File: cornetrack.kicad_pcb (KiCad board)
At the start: 2 copper layers, 275.5 x 114.5 mm, 186 parts, among them J1 MJ-4PP-9, J2 OLED, J3 MJ-4PP-9, J4 OLED, SW1 SW_PUSH, SW10 SW_PUSH, SW11 SW_PUSH, SW12 SW_PUSH, SW13 SW_PUSH, SW14 SW_PUSH, SW15 SW_PUSH, SW16 SW_PUSH, SW17 SW_PUSH, SW18 SW_PUSH, SW19 SW_PUSH, SW2 SW_PUSH, SW20 SW_PUSH, SW21 SW_PUSH, SW22 SW_PUSH, SW23 SW_PUSH, SW24 SW_PUSH, SW25 SW_PUSH, SW26 SW_PUSH, SW27 SW_PUSH, SW28 SW_PUSH, SW29 SW_PUSH, SW3 SW_PUSH, SW30 SW_PUSH, SW31 SW_PUSH, SW32 SW_PUSH, SW33 SW_PUSH, SW34 SW_PUSH, SW35 SW_PUSH, SW36 SW_PUSH, SW37 SW_PUSH, SW38 SW_PUSH, SW39 SW_PUSH, SW4 SW_PUSH, SW40 SW_PUSH, SW41 SW_PUSH, SW42 SW_PUSH, SW43 SW_PUSH, SW44 SW_PUSH, SW45 SW_PUSH, SW46 SW_PUSH, SW47 SW_PUSH, SW48 SW_PUSH, SW5 SW_PUSH, SW6 SW_PUSH, SW7 SW_PUSH, SW8 SW_PUSH, SW9 SW_PUSH, U1 ProMicro, U2 ProMicro

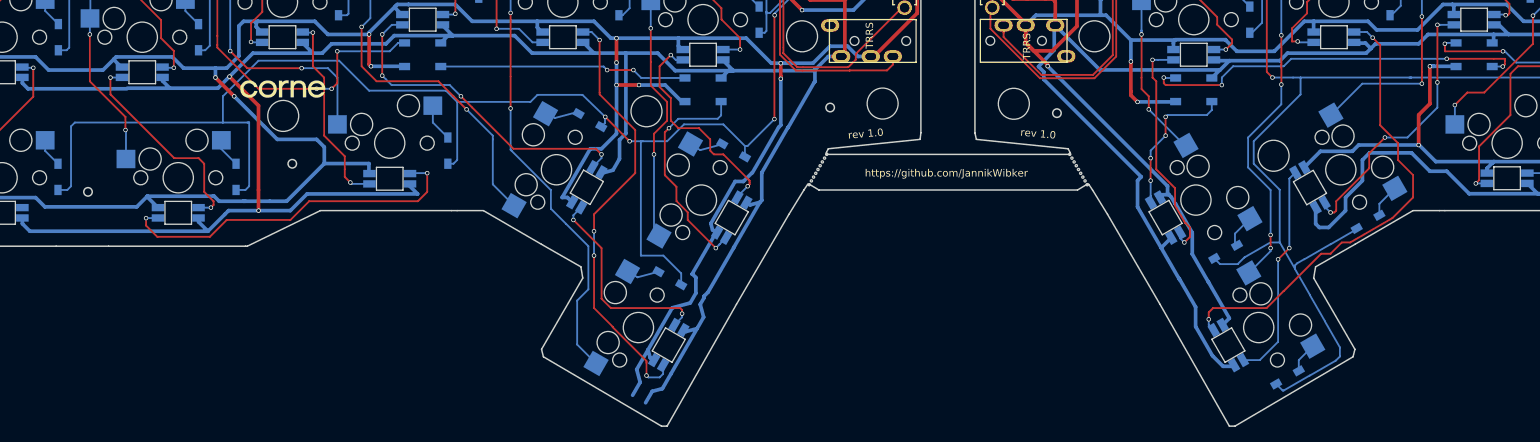
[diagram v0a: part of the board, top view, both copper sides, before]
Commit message: renamed project, diode rotation, assembly - renamed project from corne-cherry to cornetrack - tried to have all diodes rotated the same way - did numerous assembly related shenanigans; this is all in an attempt to get jlcpcb to properly detect component orientation
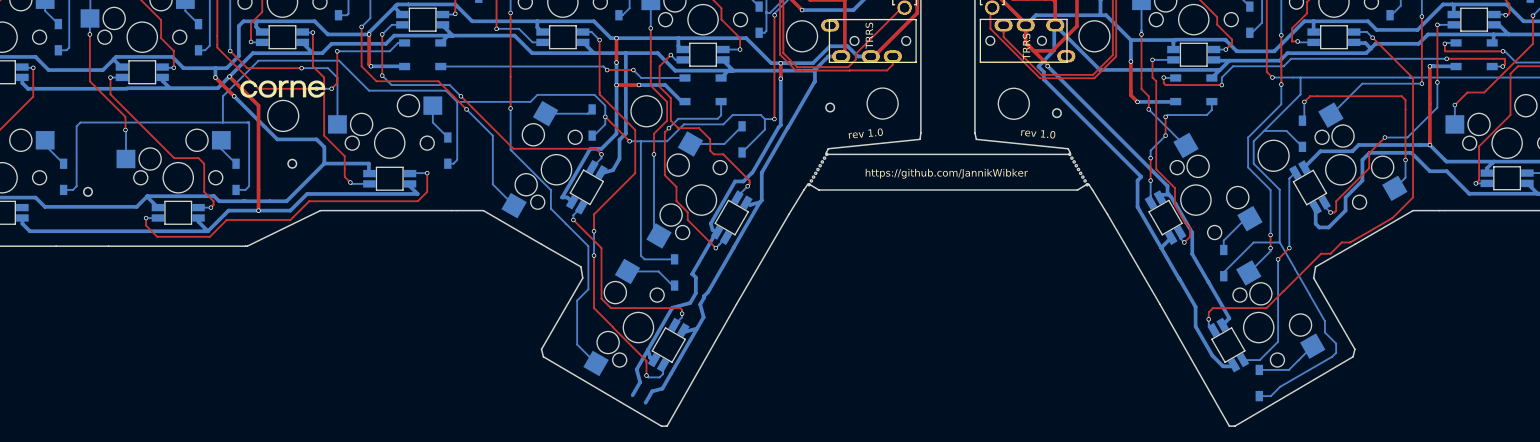
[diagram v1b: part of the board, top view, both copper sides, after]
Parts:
- moved D40 14.9 mm to (196.3, 86.9), turned to 90 degrees
- moved D41 3.89 mm to (190.5, 120.7), turned to 90 degrees
- moved D21 1.87 mm to (120.4, 87.6), turned to 90 degrees
- moved D42 1.55 mm to (185.7, 104.4), turned to 90 degrees
- moved D20 1.01 mm to (111.3, 105.7), turned to 270 degrees
- moved D43 0.76 mm to (28.4, 92.7)
- moved D19 0.44 mm to (100.1, 85.3), turned to 90 degrees
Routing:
- net Net-(D40-Pad2): track 4.52 -> 29.5 mm, vias 0 -> 2
- net Net-(D41-Pad2): track 4.13 -> 8.57 mm
- net Net-(D21-Pad2): track 4.62 -> 7.99 mm
- net row3_r: track 241.1 -> 238.3 mm
- net Net-(D20-Pad2): track 4.51 -> 7.17 mm
- net Net-(D19-Pad2): track 4.80 -> 6.55 mm
- net Net-(D42-Pad2): track 4.56 -> 6.06 mm
- net row3: track 212.5 -> 213.8 mm
- net GNDA: track 726.5 -> 725.9 mm

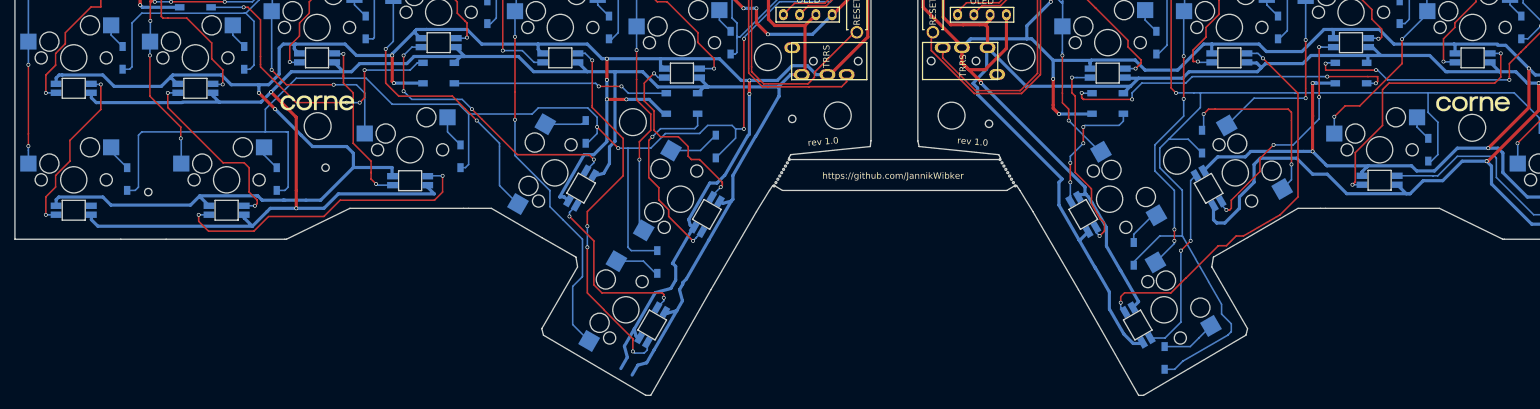
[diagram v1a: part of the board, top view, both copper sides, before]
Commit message: added bottom-plate as subproject (has no real schematic; only pcb)
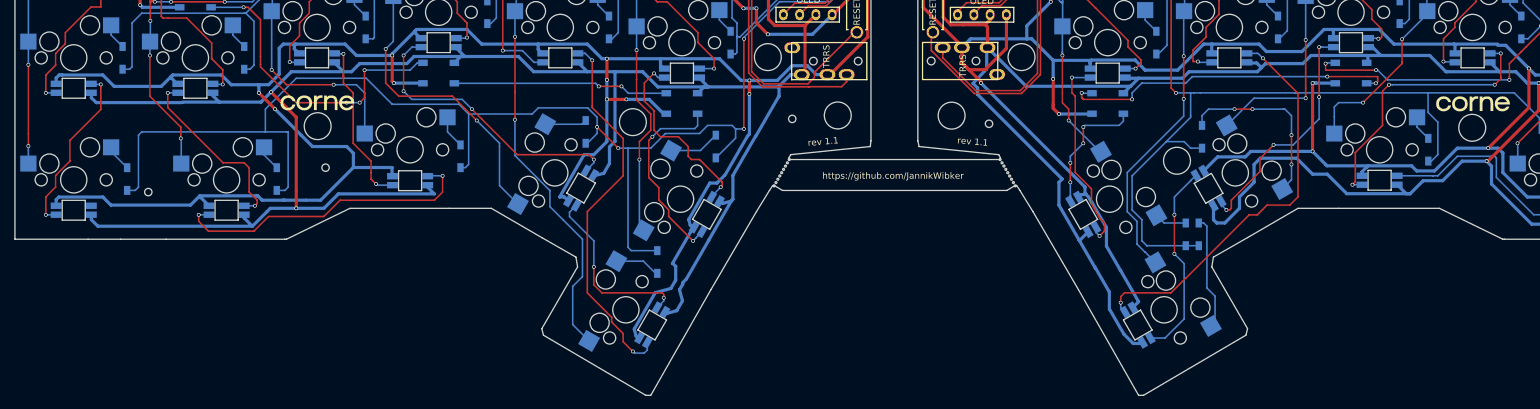
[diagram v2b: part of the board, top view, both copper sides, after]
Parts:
- added ?: , , F.Cu at (142.7, 185.2)
- moved D41 20.0 mm to (195.8, 101.3)
- moved D42 8.68 mm to (193.8, 101.3)
- moved D40 0.76 mm to (196.3, 86.1)
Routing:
- net row3_r: track 238.3 -> 209.4 mm
- net VCC: track 610.7 -> 598.1 mm
- net Net-(D41-Pad2): track 8.57 -> 17.8 mm
- net GND: track 725.7 -> 718.8 mm
- net Net-(LED52-Pad4): track 29.7 -> 31.0 mm
- net col4_r: track 130.4 -> 131.5 mm, vias 8 -> 6
- net Net-(D40-Pad2): track 29.5 -> 28.4 mm, vias 2 -> 4
- net Net-(D42-Pad2): track 6.06 -> 5.07 mm
- net col2_r: track 159.1 -> 160.0 mm
- net Net-(LED48-Pad2): vias 2 -> 4
- net Net-(LED23-Pad2): vias 4 -> 2
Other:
- outline, holes or cut-outs redrawn
- board text added: "rev 1.1"
- board text removed: "rev 1.0"

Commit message: regenerated gerber files
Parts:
- moved D21 19.5 mm to (105.4, 100.1)
- moved D20 9.66 mm to (103.4, 100.1), turned to 90 degrees
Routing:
- net row3: track 213.8 -> 204.5 mm, vias 4 -> 6
- net Net-(D21-Pad2): track 7.99 -> 16.9 mm
- net Net-(D20-Pad2): track 7.17 -> 10.2 mm
- net Net-(LED24-Pad4): track 30.3 -> 27.9 mm
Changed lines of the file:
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@@
-(kicad_pcb (version 20171130) (host pcbnew "(5.1.6-0-10_14)")
+(kicad_pcb (version 20171130) (host pcbnew "(5.1.5-rc2)")
   (general
     (thickness 1.6)
     (drawings 351)
-    (tracks 3212)
+    (tracks 3214)
     (zones 0)
     (modules 187)
@@
       (drillshape 0)
       (scaleselection 1)
-      (outputdirectory "assembly/"))
+      (outputdirectory "./"))
   )
   (net 0 "")
@@
   (module "" (layer F.Cu)
     (at 142.748 185.166)
+    (attr smd)
     (fp_text reference "" (at 145.288 185.42) (layer F.SilkS)
       (effects (font (size 1.27 1.27) (thickness 0.15)))
@@
   )
   (module kbd:D3_SMD_v2 (layer B.Cu)
-    (at 111.252 105.664 270)
+    (at 103.378 100.076 90)
     (descr "Resitance 3 pas")
     (tags R)
@@
     (fp_line (start 2.7 0.75) (end -2.7 0.75) (layer B.SilkS) (width 0.15))
     (fp_line (start -2.7 -0.75) (end 2.7 -0.75) (layer B.SilkS) (width 0.15))
-    (pad 2 smd rect (at 1.775 0 270) (size 1.4 1) (layers B.Cu B.Paste B.Mask)
+    (pad 2 smd rect (at 1.775 0 90) (size 1.4 1) (layers B.Cu B.Paste B.Mask)
       (net 24 "Net-(D20-Pad2)"))
-    (pad 1 smd rect (at -1.775 0 270) (size 1.4 1) (layers B.Cu B.Paste B.Mask)
+    (pad 1 smd rect (at -1.775 0 90) (size 1.4 1) (layers B.Cu B.Paste B.Mask)
       (net 7 row3))
     (model ${KIGITHUB3D}/Diode_SMD.3dshapes/D_SOD-123.step
@@
   )
   (module kbd:D3_SMD_v2 (layer B.Cu)
-    (at 120.396 87.63 90)
+    (at 105.41 100.076 90)
     (descr "Resitance 3 pas")
     (tags R)
@@
   (segment (start 100.333 87.119) (end 101.854 85.598) (width 0.25) (layer B.Cu) (net 7))
   (segment (start 100.076 87.119) (end 100.333 87.119) (width 0.25) (layer B.Cu) (net 7))
-  (segment (start 123.487999 84.879999) (end 124.782499 84.879999) (width 0.25) (layer B.Cu) (net 7))
-  (segment (start 119.126 84.328) (end 122.936 84.328) (width 0.25) (layer B.Cu) (net 7))
+  (segment (start 106.68 87.884) (end 106.68 93.541) (width 0.25) (layer B.Cu) (net 7))
+  (segment (start 124.064498 85.598) (end 124.782499 84.879999) (width 0.25) (layer B.Cu) (net 7))
+  (segment (start 112.522 85.598) (end 124.064498 85.598) (width 0.25) (layer B.Cu) (net 7))
   (segment (start 110.236 87.884) (end 112.522 85.598) (width 0.25) (layer B.Cu) (net 7))
-  (segment (start 117.856 85.598) (end 119.126 84.328) (width 0.25) (layer B.Cu) (net 7))
-  (segment (start 122.936 84.328) (end 123.487999 84.879999) (width 0.25) (layer B.Cu) (net 7))
-  (segment (start 112.522 85.598) (end 117.856 85.598) (width 0.25) (layer B.Cu) (net 7))
   (segment (start 105.156 87.884) (end 110.236 87.884) (width 0.25) (layer B.Cu) (net 7))
-  (segment (start 123.487999 86.313001) (end 120.396 89.405) (width 0.25) (layer B.Cu) (net 7))
-  (segment (start 123.487999 84.879999) (end 123.487999 86.313001) (width 0.25) (layer B.Cu) (net 7))
-  (segment (start 107.191 103.889) (end 111.252 103.889) (width 0.25) (layer B.Cu) (net 7))
-  (segment (start 106.68 103.378) (end 107.191 103.889) (width 0.25) (layer B.Cu) (net 7))
-  (segment (start 106.68 87.884) (end 106.68 103.378) (width 0.25) (layer B.Cu) (net 7))
+  (segment (start 102.87 101.851) (end 104.902 101.851) (width 0.25) (layer B.Cu) (net 7))
+  (segment (start 106.68 93.541) (end 106.68 96.774) (width 0.25) (layer B.Cu) (net 7))
+  (segment (start 106.68 96.774) (end 106.68 96.774) (width 0.25) (layer B.Cu) (net 7))
+  (via (at 106.68 96.774) (size 0.6) (drill 0.4) (layers F.Cu B.Cu) (net 7))
+  (segment (start 106.68 96.774) (end 106.68 101.854) (width 0.25) (layer F.Cu) (net 7))
+  (segment (start 106.68 101.854) (end 106.68 101.854) (width 0.25) (layer F.Cu) (net 7))
+  (via (at 106.68 101.854) (size 0.6) (drill 0.4) (layers F.Cu B.Cu) (net 7))
+  (segment (start 106.677 101.851) (end 106.68 101.854) (width 0.25) (layer B.Cu) (net 7))
+  (segment (start 105.41 101.851) (end 106.677 101.851) (width 0.25) (layer B.Cu) (net 7))
   (segment (start 82.9495 25.122) (end 84.7075 26.88) (width 0.25) (layer B.Cu) (net 8))
   (segment (start 82.9495 23.575) (end 82.9495 25.122) (width 0.25) (layer B.Cu) (net 8))
@@
   (segment (start 99.498696 84.146304) (end 100.076 83.569) (width 0.25) (layer B.Cu) (net 23))
   (segment (start 93.765091 84.146304) (end 99.498696 84.146304) (width 0.25) (layer B.Cu) (net 23))
-  (segment (start 111.252 107.439) (end 110.995 107.439) (width 0.25) (layer B.Cu) (net 24))
-  (segment (start 109.088997 105.532997) (end 104.870091 105.532997) (width 0.25) (layer B.Cu) (net 24))
-  (segment (start 110.995 107.439) (end 109.088997 105.532997) (width 0.25) (layer B.Cu) (net 24))
-  (segment (start 117.996289 88.254711) (end 120.396 85.855) (width 0.25) (layer B.Cu) (net 25))
-  (segment (start 113.404091 88.254711) (end 117.996289 88.254711) (width 0.25) (layer B.Cu) (net 25))
+  (segment (start 102.359 98.301) (end 103.378 98.301) (width 0.25) (layer B.Cu) (net 24))
+  (segment (start 102.108 98.552) (end 102.359 98.301) (width 0.25) (layer B.Cu) (net 24))
+  (segment (start 102.108 103.886) (end 102.108 98.552) (width 0.25) (layer B.Cu) (net 24))
+  (segment (start 103.754997 105.532997) (end 102.108 103.886) (width 0.25) (layer B.Cu) (net 24))
+  (segment (start 104.870091 105.532997) (end 103.754997 105.532997) (width 0.25) (layer B.Cu) (net 24))
+  (segment (start 107.696 97.282) (end 106.677 98.301) (width 0.25) (layer B.Cu) (net 25))
+  (segment (start 107.696 89.154) (end 107.696 97.282) (width 0.25) (layer B.Cu) (net 25))
+  (segment (start 108.204 88.646) (end 107.696 89.154) (width 0.25) (layer B.Cu) (net 25))
+  (segment (start 111.960715 88.254711) (end 111.569426 88.646) (width 0.25) (layer B.Cu) (net 25))
+  (segment (start 111.569426 88.646) (end 108.204 88.646) (width 0.25) (layer B.Cu) (net 25))
+  (segment (start 113.404091 88.254711) (end 111.960715 88.254711) (width 0.25) (layer B.Cu) (net 25))
+  (segment (start 106.677 98.301) (end 105.41 98.301) (width 0.25) (layer B.Cu) (net 25))
   (segment (start 125.349668 85.993773) (end 121.793668 92.152946) (width 0.5) (layer B.Cu) (net 26))
   (segment (start 113.62304 105.888072) (end 116.911171 100.192862) (width 0.5) (layer B.Cu) (net 26))
@@
   (via (at 110.744 76.2) (size 0.6) (drill 0.4) (layers F.Cu B.Cu) (net 99))
   (segment (start 119.764903 95.497461) (end 119.764903 95.119097) (width 0.25) (layer B.Cu) (net 99))
-  (segment (start 117.856 89.662) (end 121.412 93.218) (width 0.25) (layer F.Cu) (net 99))
-  (segment (start 121.412 93.218) (end 121.412 93.472) (width 0.25) (layer F.Cu) (net 99))
-  (segment (start 116.078 89.154) (end 116.586 89.662) (width 0.25) (layer F.Cu) (net 99))
-  (segment (start 114.554 86.106) (end 116.078 87.63) (width 0.25) (layer F.Cu) (net 99))
-  (segment (start 110.744 82.042) (end 110.744 85.09) (width 0.25) (layer F.Cu) (net 99))
-  (segment (start 116.078 87.63) (end 116.078 89.154) (width 0.25) (layer F.Cu) (net 99))
-  (segment (start 109.22 80.518) (end 110.744 82.042) (width 0.25) (layer F.Cu) (net 99))
-  (segment (start 109.22 77.724) (end 109.22 80.518) (width 0.25) (layer F.Cu) (net 99))
-  (segment (start 110.744 85.09) (end 111.76 86.106) (width 0.25) (layer F.Cu) (net 99))
-  (segment (start 116.586 89.662) (end 117.856 89.662) (width 0.25) (layer F.Cu) (net 99))
-  (segment (start 111.76 86.106) (end 114.554 86.106) (width 0.25) (layer F.Cu) (net 99))
-  (segment (start 110.744 76.2) (end 109.22 77.724) (width 0.25) (layer F.Cu) (net 99))
-  (segment (start 121.412 93.472) (end 121.412 93.726) (width 0.25) (layer F.Cu) (net 99))
-  (segment (start 121.412 93.726) (end 121.158 93.98) (width 0.25) (layer F.Cu) (net 99))
   (segment (start 121.158 93.98) (end 121.158 93.98) (width 0.25) (layer F.Cu) (net 99))
   (via (at 121.158 93.98) (size 0.6) (drill 0.4) (layers F.Cu B.Cu) (net 99))
   (segment (start 119.764903 95.373097) (end 121.158 93.98) (width 0.25) (layer B.Cu) (net 99))
   (segment (start 119.764903 95.497461) (end 119.764903 95.373097) (width 0.25) (layer B.Cu) (net 99))
+  (segment (start 109.22 77.724) (end 110.744 76.2) (width 0.25) (layer F.Cu) (net 99))
+  (segment (start 110.744 82.042) (end 109.22 80.518) (width 0.25) (layer F.Cu) (net 99))
+  (segment (start 121.412 93.218) (end 110.744 82.55) (width 0.25) (layer F.Cu) (net 99))
+  (segment (start 121.412 93.726) (end 121.412 93.218) (width 0.25) (layer F.Cu) (net 99))
+  (segment (start 110.744 82.55) (end 110.744 82.042) (width 0.25) (layer F.Cu) (net 99))
+  (segment (start 109.22 80.518) (end 109.22 77.724) (width 0.25) (layer F.Cu) (net 99))
+  (segment (start 121.158 93.98) (end 121.412 93.726) (width 0.25) (layer F.Cu) (net 99))
   (segment (start 98.588339 96.852194) (end 97.536 97.904533) (width 0.25) (layer B.Cu) (net 100))
   (segment (start 97.536 97.904533) (end 97.536 98.552) (width 0.25) (layer B.Cu) (net 100))

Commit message: made all holes and almost all diodes on both pcbs symmetric to each other (meaning that accidentally having all coordinates in the .pos file inverted would not cause a big problem for almost all of the diodes)
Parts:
- removed the Ref** at (191.1, 41.8)
- removed the Ref** at (267.1, 45.3)
- removed the Ref** at (238.5, 84.7)
- removed the Ref** at (192.4, 89.8)
- added G***: LOGO, kbd:corne-logo-horizontal, B.Cu at (502.5, 165.1)
- added G***: LOGO, kbd:corne-logo-horizontal, F.Cu at (502.7, 165.1)
- added Ref**: Val**, kbd:M2_HOLE_v2, B.Cu at (421.1, 166.9)
- added Ref**: Val**, kbd:M2_HOLE_v2, B.Cu at (267.0, 45.2)
- added Ref**: Val**, kbd:M2_HOLE_v2, B.Cu at (191.1, 41.8)
- added Ref**: Val**, kbd:M2_HOLE_v2, B.Cu at (238.5, 84.4)
- added Ref**: Val**, kbd:M2_HOLE_v2, B.Cu at (189.2, 83.8)
- added Ref**: Val**, kbd:M2_HOLE_v2, B.Cu at (432.1, 157.7)
- added Ref**: Val**, kbd:M2_HOLE_v2, B.Cu at (530.9, 129.3)
- added Ref**: Val**, kbd:M2_HOLE_v2, B.Cu at (455.0, 125.8)
- added Ref**: Val**, kbd:M2_HOLE_v2, B.Cu at (502.4, 168.5)
- added Ref**: Val**, kbd:M2_HOLE_v2, B.Cu at (453.1, 167.9)
- added Ref**: Val**, kbd:M2_HOLE_v2, B.Cu at (532.2, 166.5)
- added Ref**: Val**, kbd:M2_HOLE_v2, B.Cu at (268.3, 82.4)
- added Ref**: Val**, kbd:M2_HOLE_v2, F.Cu at (28.4, 82.4)
- added SW22: SW_PUSH, kbd:CherryMX_Hotswap, F.Cu at (540.5, 119.8)
- added SW23: SW_PUSH, kbd:CherryMX_Hotswap, F.Cu at (521.5, 119.8)
- added SW24: SW_PUSH, kbd:CherryMX_Hotswap, F.Cu at (502.5, 115.1)
- added SW25: SW_PUSH, kbd:CherryMX_Hotswap, F.Cu at (483.5, 112.7)
- added SW26: SW_PUSH, kbd:CherryMX_Hotswap, F.Cu at (464.5, 115.1)
- added SW27: SW_PUSH, kbd:CherryMX_Hotswap, F.Cu at (445.5, 117.5)
- added SW28: SW_PUSH, kbd:CherryMX_Hotswap, F.Cu at (540.5, 138.8)
- added SW29: SW_PUSH, kbd:CherryMX_Hotswap, F.Cu at (521.5, 138.8)
- added SW30: SW_PUSH, kbd:CherryMX_Hotswap, F.Cu at (502.5, 134.1)
- added SW31: SW_PUSH, kbd:CherryMX_Hotswap, F.Cu at (483.5, 131.7)
- added SW32: SW_PUSH, kbd:CherryMX_Hotswap, F.Cu at (464.5, 134.1)
- added SW33: SW_PUSH, kbd:CherryMX_Hotswap, F.Cu at (445.5, 136.5)
- added SW34: SW_PUSH, kbd:CherryMX_Hotswap, F.Cu at (540.5, 157.8)
- added SW35: SW_PUSH, kbd:CherryMX_Hotswap, F.Cu at (521.5, 157.8)
- added SW36: SW_PUSH, kbd:CherryMX_Hotswap, F.Cu at (502.5, 153.1)
- added SW37: SW_PUSH, kbd:CherryMX_Hotswap, F.Cu at (483.5, 150.7)
- added SW38: SW_PUSH, kbd:CherryMX_Hotswap, F.Cu at (464.5, 153.1)
- added SW39: SW_PUSH, kbd:CherryMX_Hotswap, F.Cu at (445.5, 155.5)
- added SW40: SW_PUSH, kbd:CherryMX_Hotswap, F.Cu at (465.4, 175.8)
- added SW41: SW_PUSH, kbd:CherryMX_Hotswap, F.Cu at (454.3, 197.2)
- added SW42: SW_PUSH, kbd:CherryMX_Hotswap, F.Cu at (445.8, 179.9)
- added SW46: SW_PUSH, kbd:CherryMX_Hotswap, F.Cu at (535.7, 176.9)
- added SW47: SW_PUSH, kbd:CherryMX_Hotswap, F.Cu at (516.6, 176.9)
- added SW48: SW_PUSH, kbd:CherryMX_Hotswap, F.Cu at (488.0, 172.2)
- moved D46 3.84 mm to (283.2, 92.2)
- moved D45 1.01 mm to (80.5, 88.1)
- moved D43 0.72 mm to (29.0, 92.2)
- moved D33 0.34 mm to (189.2, 52.1)
- moved D24 0.29 mm to (246.2, 30.7)
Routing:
- net row3: track 204.5 -> 199.4 mm
- net Net-(LED58-Pad4): track 30.0 -> 25.7 mm
- net Net-(D46-Pad2): track 3.93 -> 7.38 mm
- net row3_r: track 209.4 -> 206.6 mm, vias 2 -> 4
- net col4_r: track 131.5 -> 134.2 mm
- net VDD: track 661.9 -> 660.7 mm, vias 4 -> 6
- net Net-(D45-Pad2): track 5.16 -> 4.15 mm
- net Net-(D43-Pad2): track 4.22 -> 4.98 mm
- net GNDA: track 725.9 -> 725.1 mm
- net row1_r: track 181.4 -> 180.7 mm
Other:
- board size 275.5 x 114.5 mm -> 539 x 198.5 mm
